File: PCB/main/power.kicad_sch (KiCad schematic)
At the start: 28 parts, among them M1 CJ2301 S1, U1 LP2951-33DR, U2 LM324

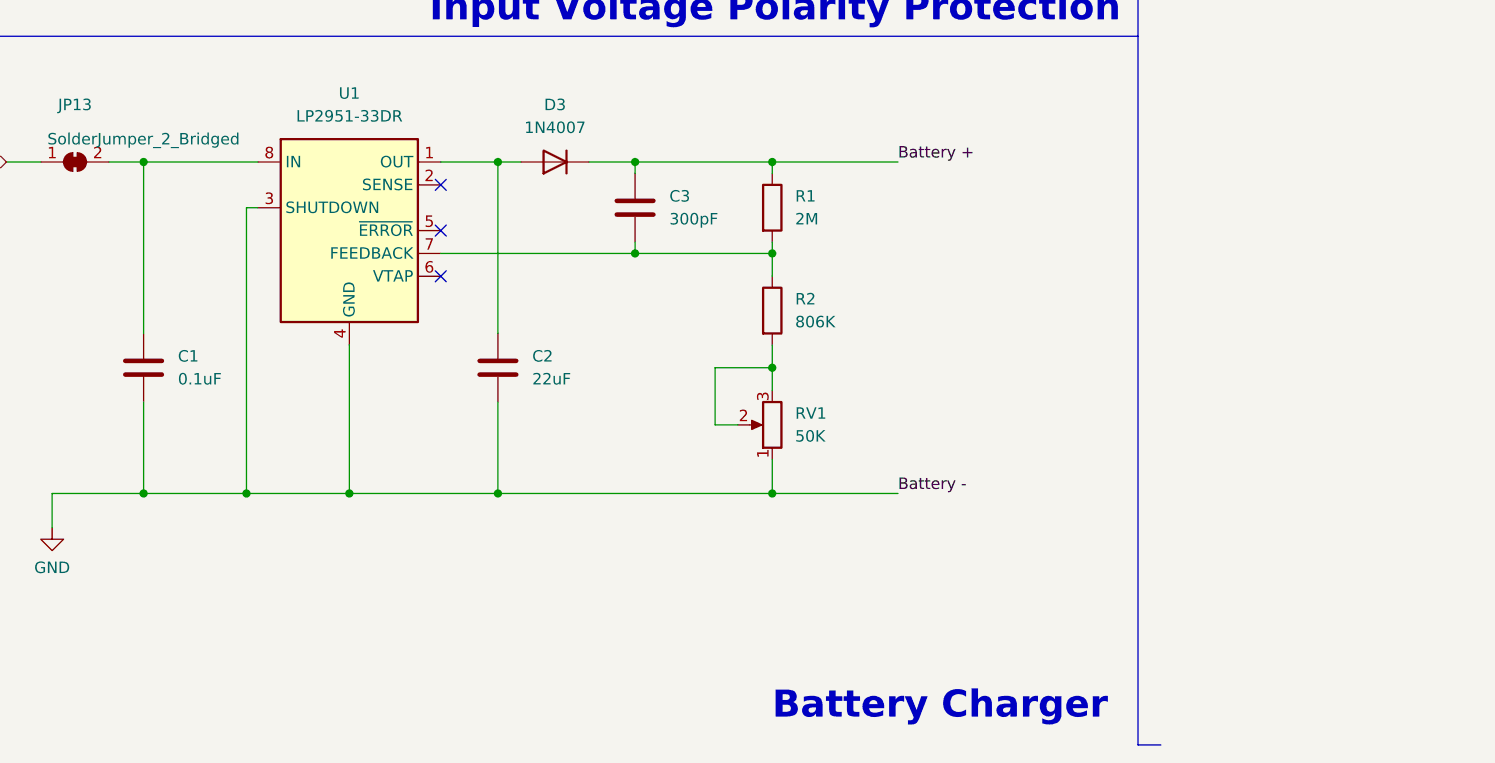
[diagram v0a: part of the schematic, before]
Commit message: Add power flags
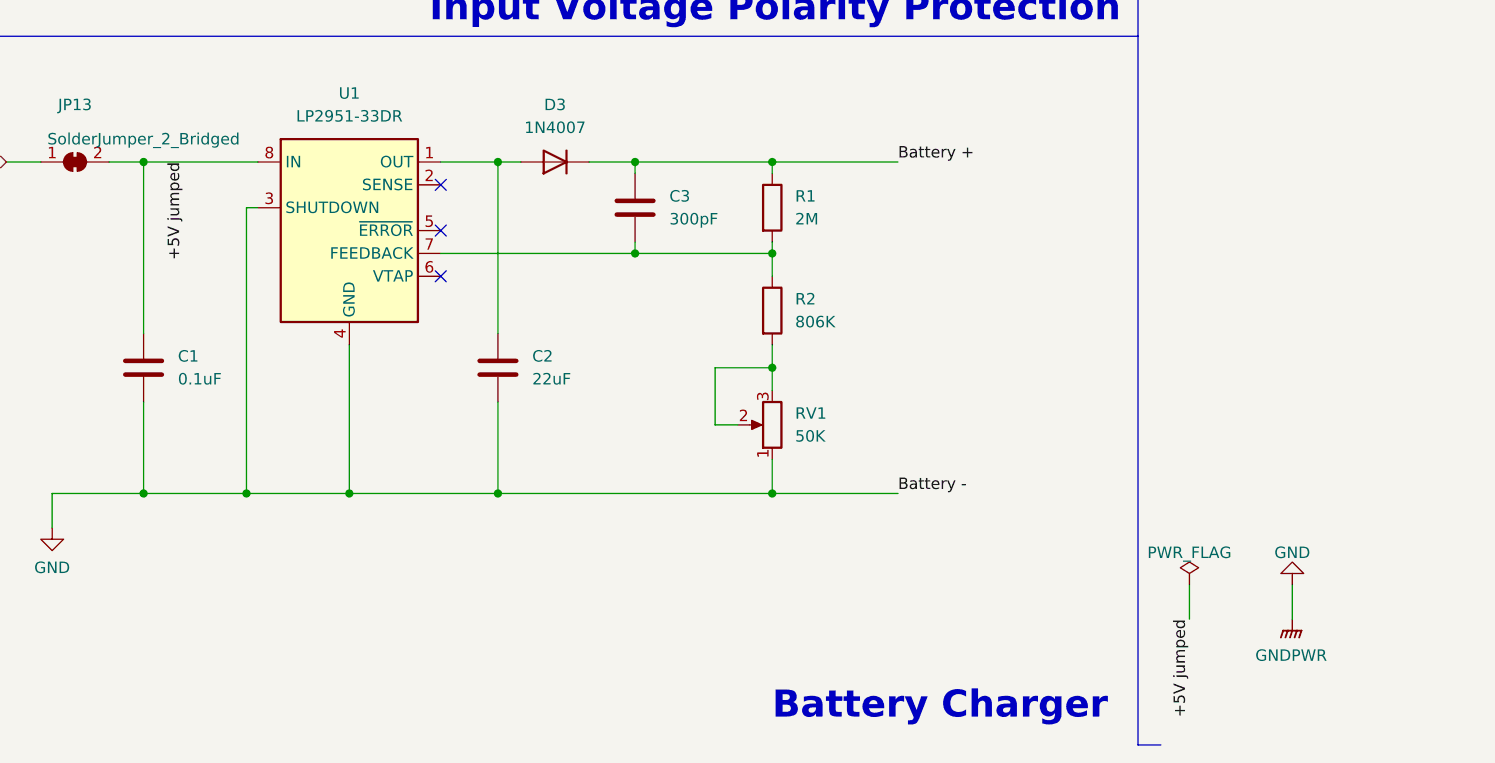
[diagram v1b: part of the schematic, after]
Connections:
- net +5V jumped: now reaches C1.1, JP13.2 (B), U1.8 (IN)
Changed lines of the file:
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@@
+    (stroke (width 0) (type default) (color 0 0 0 0))
+  )
+  (wire (pts (xy 165.735 180.34) (xy 165.735 184.15))
     (stroke (width 0) (type default) (color 0 0 0 0))
   )
@@
   )
   (wire (pts (xy 60.96 91.44) (xy 63.5 91.44))
+    (stroke (width 0) (type default) (color 0 0 0 0))
+  )
+  (wire (pts (xy 154.305 180.34) (xy 154.305 184.15))
     (stroke (width 0) (type default) (color 0 0 0 0))
   )
@@
     (effects (font (size 1.27 1.27)) (justify left bottom))
   )
+  (label "+5V jumped" (at 154.305 184.15 270)
+    (effects (font (size 1.27 1.27)) (justify right bottom))
+  )
   (label "Battery +" (at 86.36 34.29 0)
     (effects (font (size 1.27 1.27)) (justify left bottom))
@@
   (label "+5V (INPUT PROTECTED)" (at 85.09 99.06 0)
     (effects (font (size 1.27 1.27)) (justify left bottom))
+  )
+  (label "+5V jumped" (at 42.545 133.35 270)
+    (effects (font (size 1.27 1.27)) (justify right bottom))
   )
   (label "+5V (REVERSE PROTECTED)" (at 78.74 66.04 0)
@@
     )
     (property "Datasheet" "" (id 3) (at 246.38 31.75 0)
+      (effects (font (size 1.27 1.27)) hide)
+    )
+    (pin "1")
+  )
+  (symbol (lib_id "power:GNDPWR") (at 165.735 184.15 0) (unit 1)
+    (in_bom yes) (on_board yes) (fields_autoplaced)
+    (property "Reference" "#PWR017" (id 0) (at 165.735 189.23 0)
+      (effects (font (size 1.27 1.27)) hide)
+    )
+    (property "Value" "GNDPWR" (id 1) (at 165.608 188.187 0))
+    (property "Footprint" "" (id 2) (at 165.735 185.42 0)
+      (effects (font (size 1.27 1.27)) hide)
+    )
+    (property "Datasheet" "" (id 3) (at 165.735 185.42 0)
       (effects (font (size 1.27 1.27)) hide)
     )
@@
     (pin "1")
   )
+  (symbol (lib_id "power:PWR_FLAG") (at 154.305 180.34 0) (unit 1)
+    (in_bom yes) (on_board yes) (fields_autoplaced)
+    (property "Reference" "#FLG03" (id 0) (at 154.305 178.435 0)
+      (effects (font (size 1.27 1.27)) hide)
+    )
+    (property "Value" "PWR_FLAG" (id 1) (at 154.305 176.7642 0))
+    (property "Footprint" "" (id 2) (at 154.305 180.34 0)
+      (effects (font (size 1.27 1.27)) hide)
+    )
+    (property "Datasheet" "~" (id 3) (at 154.305 180.34 0)
+      (effects (font (size 1.27 1.27)) hide)
+    )
+    (pin "1")
+  )
   (symbol (lib_id "pspice:MPMOS") (at 256.54 45.72 0) (unit 1)
     (in_bom yes) (on_board yes) (fields_autoplaced)
@@
     (pin "2")
   )
+  (symbol (lib_id "power:GND") (at 165.735 180.34 180) (unit 1)
+    (in_bom yes) (on_board yes) (fields_autoplaced)
+    (property "Reference" "#PWR013" (id 0) (at 165.735 173.99 0)
+      (effects (font (size 1.27 1.27)) hide)
+    )
+    (property "Value" "GND" (id 1) (at 165.735 176.7642 0))
+    (property "Footprint" "" (id 2) (at 165.735 180.34 0)
+      (effects (font (size 1.27 1.27)) hide)
+    )
+    (property "Datasheet" "" (id 3) (at 165.735 180.34 0)
+      (effects (font (size 1.27 1.27)) hide)
+    )
+    (pin "1")
+  )
   (sheet_instances

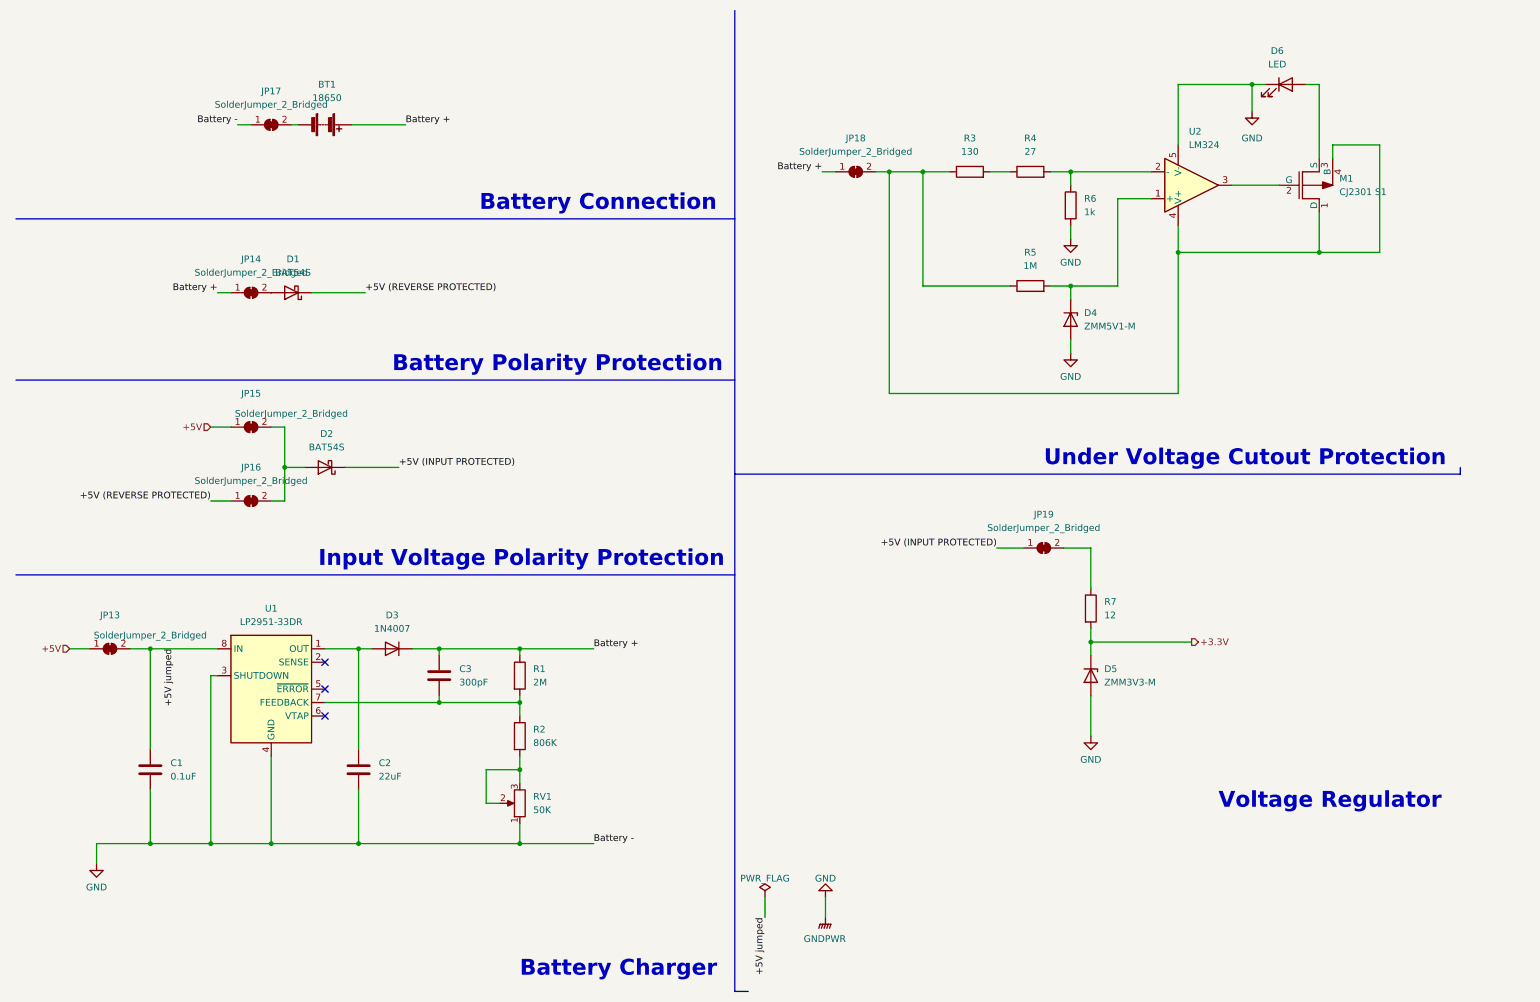
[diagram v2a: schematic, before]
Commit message: Add footprints
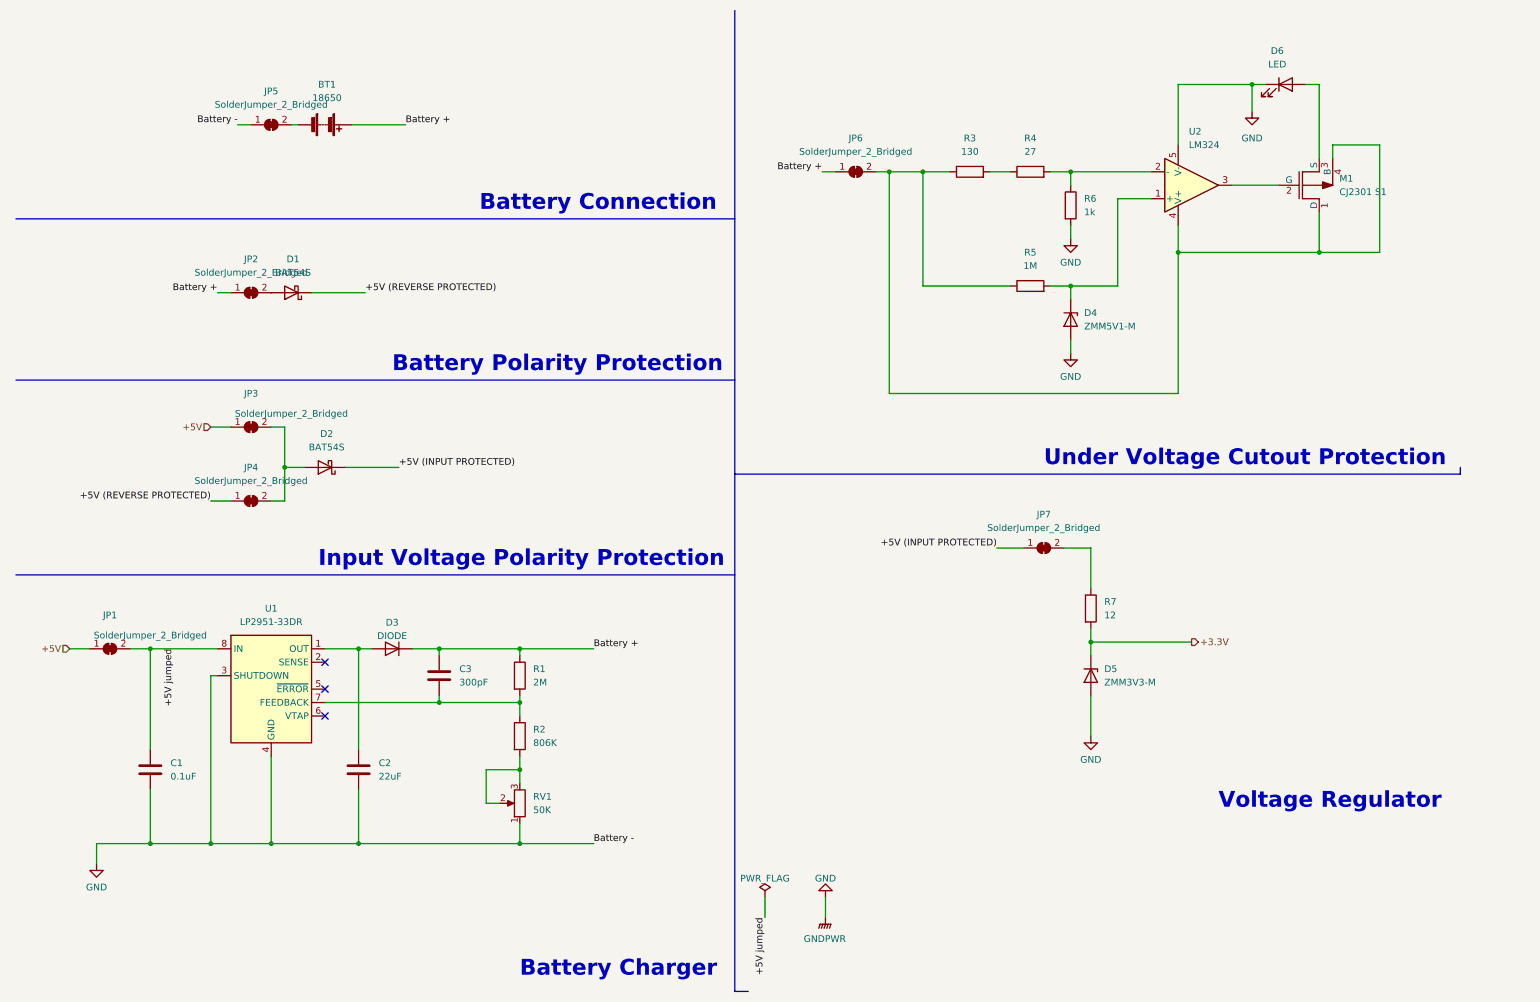
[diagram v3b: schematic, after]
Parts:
- removed D3: 1N4007, Diode_THT:D_DO-41_SOD81_P10.16mm_Horizontal, symbol Diode:1N4007
- added D3: DIODE, Diode_SMD:D_SMA, symbol Simulation_SPICE:DIODE
- BT1: footprint (none) -> Footprint_EEE3088F:18650_Holder
- D4, D5: footprint (none) -> Footprint_EEE3088F:LL-34_L3.5-W1.5-RD
- M1: footprint (none) -> Package_TO_SOT_SMD:SOT-23
- RV1: footprint (none) -> Footprint_EEE3088F:VG039NCHXTB503
- renumbered JP13 to JP1, JP14 to JP2, JP15 to JP3, JP16 to JP4, JP17 to JP5, JP18 to JP6, JP19 to JP7
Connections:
- net Battery +: now also D3.2 (K)
- net at C2.1, U1.1 (OUT): now also D3.1 (A)
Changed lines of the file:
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@@
   (symbol (lib_id "Jumper:SolderJumper_2_Bridged") (at 60.96 34.29 0) (unit 1)
     (in_bom yes) (on_board yes) (fields_autoplaced)
-    (property "Reference" "JP17" (id 0) (at 60.96 27.94 0))
+    (property "Reference" "JP5" (id 0) (at 60.96 27.94 0))
     (property "Value" "SolderJumper_2_Bridged" (id 1) (at 60.96 30.48 0))
     (property "Footprint" "Jumper:SolderJumper-2_P1.3mm_Bridged2Bar_Pad1.0x1.5mm" (id 2) (at 60.96 34.29 0)
@@
   (symbol (lib_id "power:GND") (at 215.9 149.86 0) (unit 1)
     (in_bom yes) (on_board yes) (fields_autoplaced)
-    (property "Reference" "#PWR023" (id 0) (at 215.9 156.21 0)
+    (property "Reference" "#PWR020" (id 0) (at 215.9 156.21 0)
       (effects (font (size 1.27 1.27)) hide)
     )
@@
   (symbol (lib_id "Jumper:SolderJumper_2_Bridged") (at 207.01 114.3 0) (unit 1)
     (in_bom yes) (on_board yes) (fields_autoplaced)
-    (property "Reference" "JP19" (id 0) (at 207.01 107.95 0))
+    (property "Reference" "JP7" (id 0) (at 207.01 107.95 0))
     (property "Value" "SolderJumper_2_Bridged" (id 1) (at 207.01 110.49 0))
     (property "Footprint" "Jumper:SolderJumper-2_P1.3mm_Bridged2Bar_Pad1.0x1.5mm" (id 2) (at 207.01 114.3 0)
@@
       (effects (font (size 1.27 1.27)) (justify left))
     )
-    (property "Footprint" "" (id 2) (at 215.9 138.43 0)
+    (property "Footprint" "Footprint_EEE3088F:LL-34_L3.5-W1.5-RD" (id 2) (at 215.9 138.43 0)
       (effects (font (size 1.27 1.27)) hide)
     )
@@
   (symbol (lib_id "power:GND") (at 212.09 55.88 0) (unit 1)
     (in_bom yes) (on_board yes) (fields_autoplaced)
-    (property "Reference" "#PWR020" (id 0) (at 212.09 62.23 0)
+    (property "Reference" "#PWR018" (id 0) (at 212.09 62.23 0)
       (effects (font (size 1.27 1.27)) hide)
     )
@@
   (symbol (lib_id "Jumper:SolderJumper_2_Bridged") (at 57.15 66.04 0) (unit 1)
     (in_bom yes) (on_board yes) (fields_autoplaced)
-    (property "Reference" "JP14" (id 0) (at 57.15 59.69 0))
+    (property "Reference" "JP2" (id 0) (at 57.15 59.69 0))
     (property "Value" "SolderJumper_2_Bridged" (id 1) (at 57.15 62.23 0))
     (property "Footprint" "Jumper:SolderJumper-2_P1.3mm_Bridged2Bar_Pad1.0x1.5mm" (id 2) (at 57.15 66.04 0)
@@
   (symbol (lib_id "Jumper:SolderJumper_2_Bridged") (at 57.15 105.41 0) (unit 1)
     (in_bom yes) (on_board yes) (fields_autoplaced)
-    (property "Reference" "JP16" (id 0) (at 57.15 99.06 0))
+    (property "Reference" "JP4" (id 0) (at 57.15 99.06 0))
     (property "Value" "SolderJumper_2_Bridged" (id 1) (at 57.15 101.6 0))
     (property "Footprint" "Jumper:SolderJumper-2_P1.3mm_Bridged2Bar_Pad1.0x1.5mm" (id 2) (at 57.15 105.41 0)
@@
   (symbol (lib_id "Jumper:SolderJumper_2_Bridged") (at 30.48 133.35 0) (unit 1)
     (in_bom yes) (on_board yes)
-    (property "Reference" "JP13" (id 0) (at 30.48 127 0))
+    (property "Reference" "JP1" (id 0) (at 30.48 127 0))
     (property "Value" "SolderJumper_2_Bridged" (id 1) (at 38.1 130.81 0))
     (property "Footprint" "Jumper:SolderJumper-2_P1.3mm_Bridged2Bar_Pad1.0x1.5mm" (id 2) (at 30.48 133.35 0)
@@
   (symbol (lib_id "Jumper:SolderJumper_2_Bridged") (at 171.45 43.18 0) (unit 1)
     (in_bom yes) (on_board yes) (fields_autoplaced)
-    (property "Reference" "JP18" (id 0) (at 171.45 36.83 0))
+    (property "Reference" "JP6" (id 0) (at 171.45 36.83 0))
     (property "Value" "SolderJumper_2_Bridged" (id 1) (at 171.45 39.37 0))
     (property "Footprint" "Jumper:SolderJumper-2_P1.3mm_Bridged2Bar_Pad1.0x1.5mm" (id 2) (at 171.45 43.18 0)
@@
     )
     (property "Datasheet" "~" (id 3) (at 171.45 43.18 0)
-      (effects (font (size 1.27 1.27)) hide)
-    )
-    (pin "1")
-    (pin "2")
-  )
-  (symbol (lib_id "Diode:1N4007") (at 83.82 133.35 180) (unit 1)
-    (in_bom yes) (on_board yes) (fields_autoplaced)
-    (property "Reference" "D3" (id 0) (at 83.82 127 0))
-    (property "Value" "1N4007" (id 1) (at 83.82 129.54 0))
-    (property "Footprint" "Diode_THT:D_DO-41_SOD81_P10.16mm_Horizontal" (id 2) (at 83.82 128.905 0)
-      (effects (font (size 1.27 1.27)) hide)
-    )
-    (property "Datasheet" "http://www.vishay.com/docs/88503/1n4001.pdf" (id 3) (at 83.82 133.35 0)
       (effects (font (size 1.27 1.27)) hide)
     )
@@
   (symbol (lib_id "power:GND") (at 27.94 173.99 0) (unit 1)
     (in_bom yes) (on_board yes) (fields_autoplaced)
-    (property "Reference" "#PWR01" (id 0) (at 27.94 180.34 0)
+    (property "Reference" "#PWR015" (id 0) (at 27.94 180.34 0)
       (effects (font (size 1.27 1.27)) hide)
     )
@@
     (property "Reference" "BT1" (id 0) (at 71.501 26.67 90))
     (property "Value" "18650" (id 1) (at 71.501 29.21 90))
-    (property "Footprint" "" (id 2) (at 72.644 34.29 90)
+    (property "Footprint" "Footprint_EEE3088F:18650_Holder" (id 2) (at 72.644 34.29 90)
       (effects (font (size 1.27 1.27)) hide)
     )
     (property "Datasheet" "~" (id 3) (at 72.644 34.29 90)
       (effects (font (size 1.27 1.27)) hide)
+    )
+    (pin "1")
+    (pin "2")
+  )
+  (symbol (lib_id "Simulation_SPICE:DIODE") (at 83.82 133.35 0) (unit 1)
+    (in_bom yes) (on_board yes) (fields_autoplaced)
+    (property "Reference" "D3" (id 0) (at 83.82 128.3802 0))
+    (property "Value" "DIODE" (id 1) (at 83.82 130.9171 0))
+    (property "Footprint" "Diode_SMD:D_SMA" (id 2) (at 83.82 133.35 0)
+      (effects (font (size 1.27 1.27)) hide)
+    )
+    (property "Datasheet" "~" (id 3) (at 83.82 133.35 0)
+      (effects (font (size 1.27 1.27)) hide)
+    )
+    (property "Spice_Netlist_Enabled" "Y" (id 4) (at 83.82 133.35 0)
+      (effects (font (size 1.27 1.27)) (justify left) hide)
+    )
+    (property "Spice_Primitive" "D" (id 5) (at 83.82 133.35 0)
+      (effects (font (size 1.27 1.27)) (justify left) hide)
     )
     (pin "1")
@@
       (effects (font (size 1.27 1.27)) (justify right))
     )
-    (property "Footprint" "" (id 2) (at 107.95 162.56 0)
+    (property "Footprint" "Footprint_EEE3088F:VG039NCHXTB503" (id 2) (at 107.95 162.56 0)
       (effects (font (size 1.27 1.27)) hide)
     )
@@
   (symbol (lib_id "power:GND") (at 212.09 77.47 0) (unit 1)
     (in_bom yes) (on_board yes) (fields_autoplaced)
-    (property "Reference" "#PWR022" (id 0) (at 212.09 83.82 0)
+    (property "Reference" "#PWR019" (id 0) (at 212.09 83.82 0)
       (effects (font (size 1.27 1.27)) hide)
     )
@@
   (symbol (lib_id "power:PWR_FLAG") (at 154.305 180.34 0) (unit 1)
     (in_bom yes) (on_board yes) (fields_autoplaced)
-    (property "Reference" "#FLG03" (id 0) (at 154.305 178.435 0)
+    (property "Reference" "#FLG01" (id 0) (at 154.305 178.435 0)
       (effects (font (size 1.27 1.27)) hide)
     )
@@
       (effects (font (size 1.27 1.27)) (justify left))
     )
-    (property "Footprint" "" (id 2) (at 256.54 45.72 0)
+    (property "Footprint" "Package_TO_SOT_SMD:SOT-23" (id 2) (at 256.54 45.72 0)
       (effects (font (size 1.27 1.27)) hide)
     )
@@
   (symbol (lib_id "Jumper:SolderJumper_2_Bridged") (at 57.15 91.44 0) (unit 1)
     (in_bom yes) (on_board yes)
-    (property "Reference" "JP15" (id 0) (at 57.15 85.09 0))
+    (property "Reference" "JP3" (id 0) (at 57.15 85.09 0))
     (property "Value" "SolderJumper_2_Bridged" (id 1) (at 64.77 88.9 0))
     (property "Footprint" "Jumper:SolderJumper-2_P1.3mm_Bridged2Bar_Pad1.0x1.5mm" (id 2) (at 57.15 91.44 0)
@@
       (effects (font (size 1.27 1.27)) (justify left))
     )
-    (property "Footprint" "" (id 2) (at 212.09 71.12 0)
+    (property "Footprint" "Footprint_EEE3088F:LL-34_L3.5-W1.5-RD" (id 2) (at 212.09 71.12 0)
       (effects (font (size 1.27 1.27)) hide)
     )
@@
   (symbol (lib_id "power:GND") (at 165.735 180.34 180) (unit 1)
     (in_bom yes) (on_board yes) (fields_autoplaced)
-    (property "Reference" "#PWR013" (id 0) (at 165.735 173.99 0)
-      (effects (font (size 1.27 1.27)) hide)
-    )
+    (property "Reference" "#PWR016" (id 0) (at 165.735 173.99 0)
+      (effects (font (size 1.27 1.27)) hide)
+    )
